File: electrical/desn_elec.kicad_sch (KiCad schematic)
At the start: 0 parts

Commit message: Update electrical
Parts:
- added BT1: Battery, symbol Device:Battery
- added J1: LOGITECH F310, symbol Connector:USB_A
- added M1, M2, M3: ESC_PWM, symbol PROJECT_SYM:ESC_PWM
- added U1: ESP32-S3-Zero, symbol PROJECT_SYM:ESP32-S3-Zero
- added U2: LM2596S-MOD, symbol PROJECT_SYM:LM2596S-MOD
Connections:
- new net: U1.18 (GND), U2. (VOUT)
- new net +5V: J1.4 (GND), J1.5 (Shield), U1.19 (5V), U1.22 (VBUS_USB), U2. (VOUT)
- new net +BATT: BT1.1 (+), M1.2 (+), M2.2 (+), M3.2 (+), U2. (VOUT)
- new net CONT_USB_D+: J1.3 (D+), U1.22 (VBUS_USB)
- new net CONT_USB_D-: J1.2 (D-), U1.22 (VBUS_USB)
- new net ESC_1: M1.4 (PWM), U1.3 (IO3)
- new net ESC_2: M2.4 (PWM), U1.2 (IO2)
- new net ESC_3: M3.4 (PWM), U1.1 (IO1)
- new net GND: BT1.2 (-), J1.1 (VBUS), M1.1 (-), M2.1 (-), M3.1 (-), U1.22 (VBUS_USB), U2. (VOUT)
- no-connect marks 0 -> 16

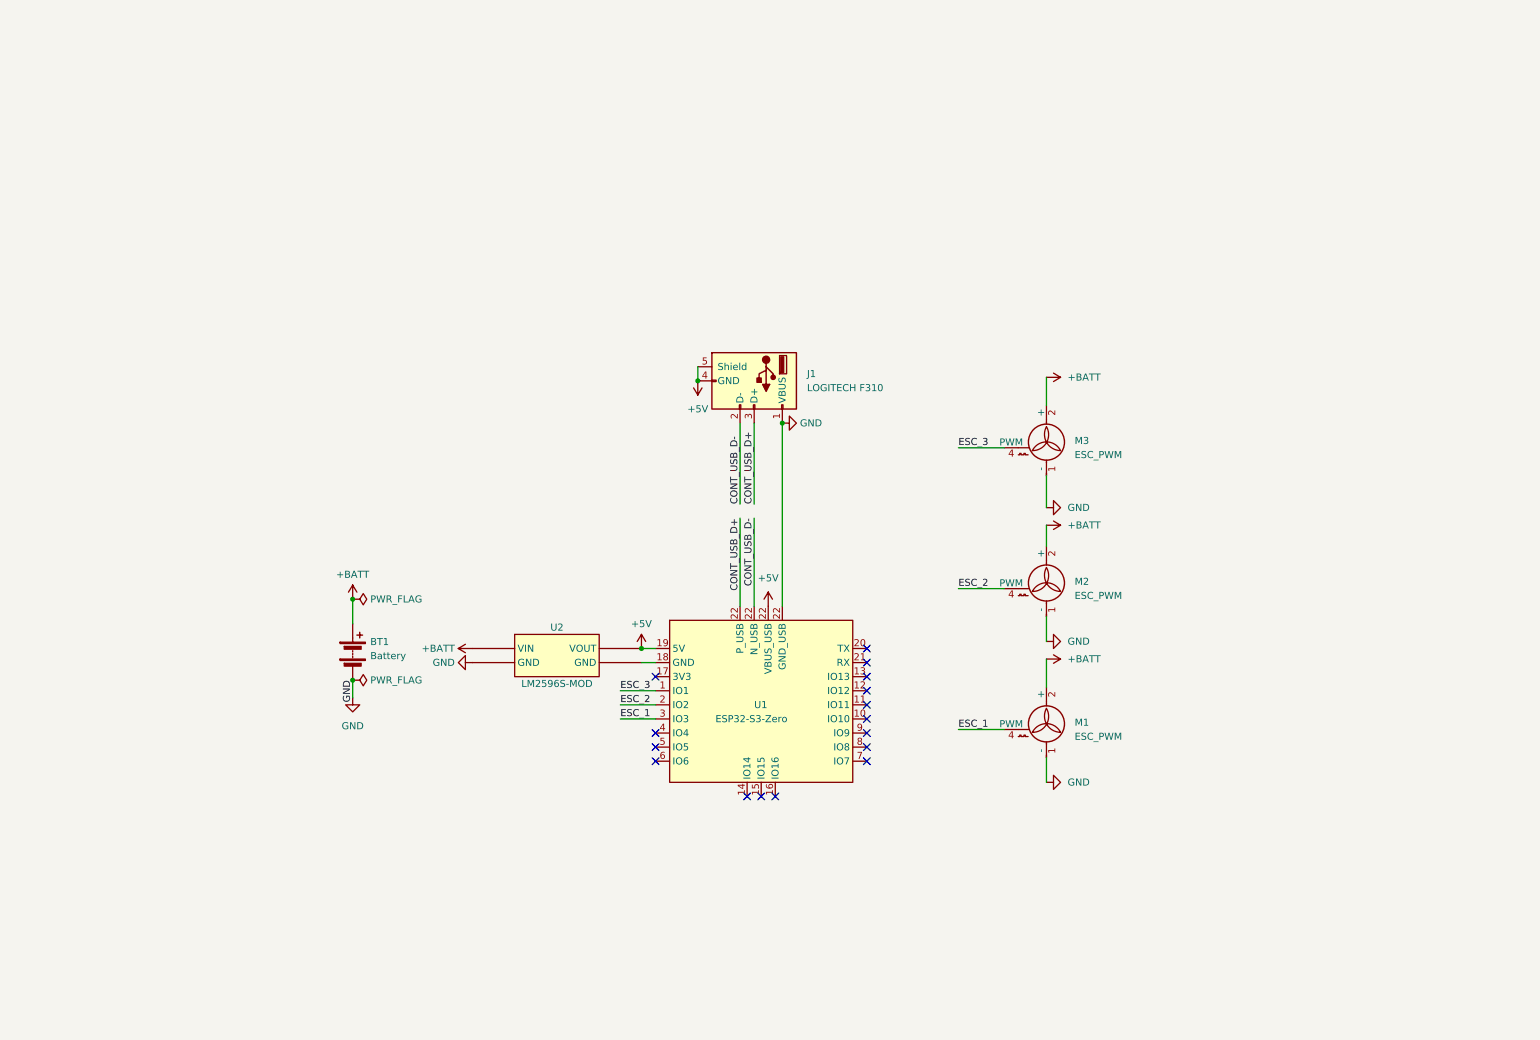
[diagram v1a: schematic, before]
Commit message: Update elec, make the diagram a bit nicer
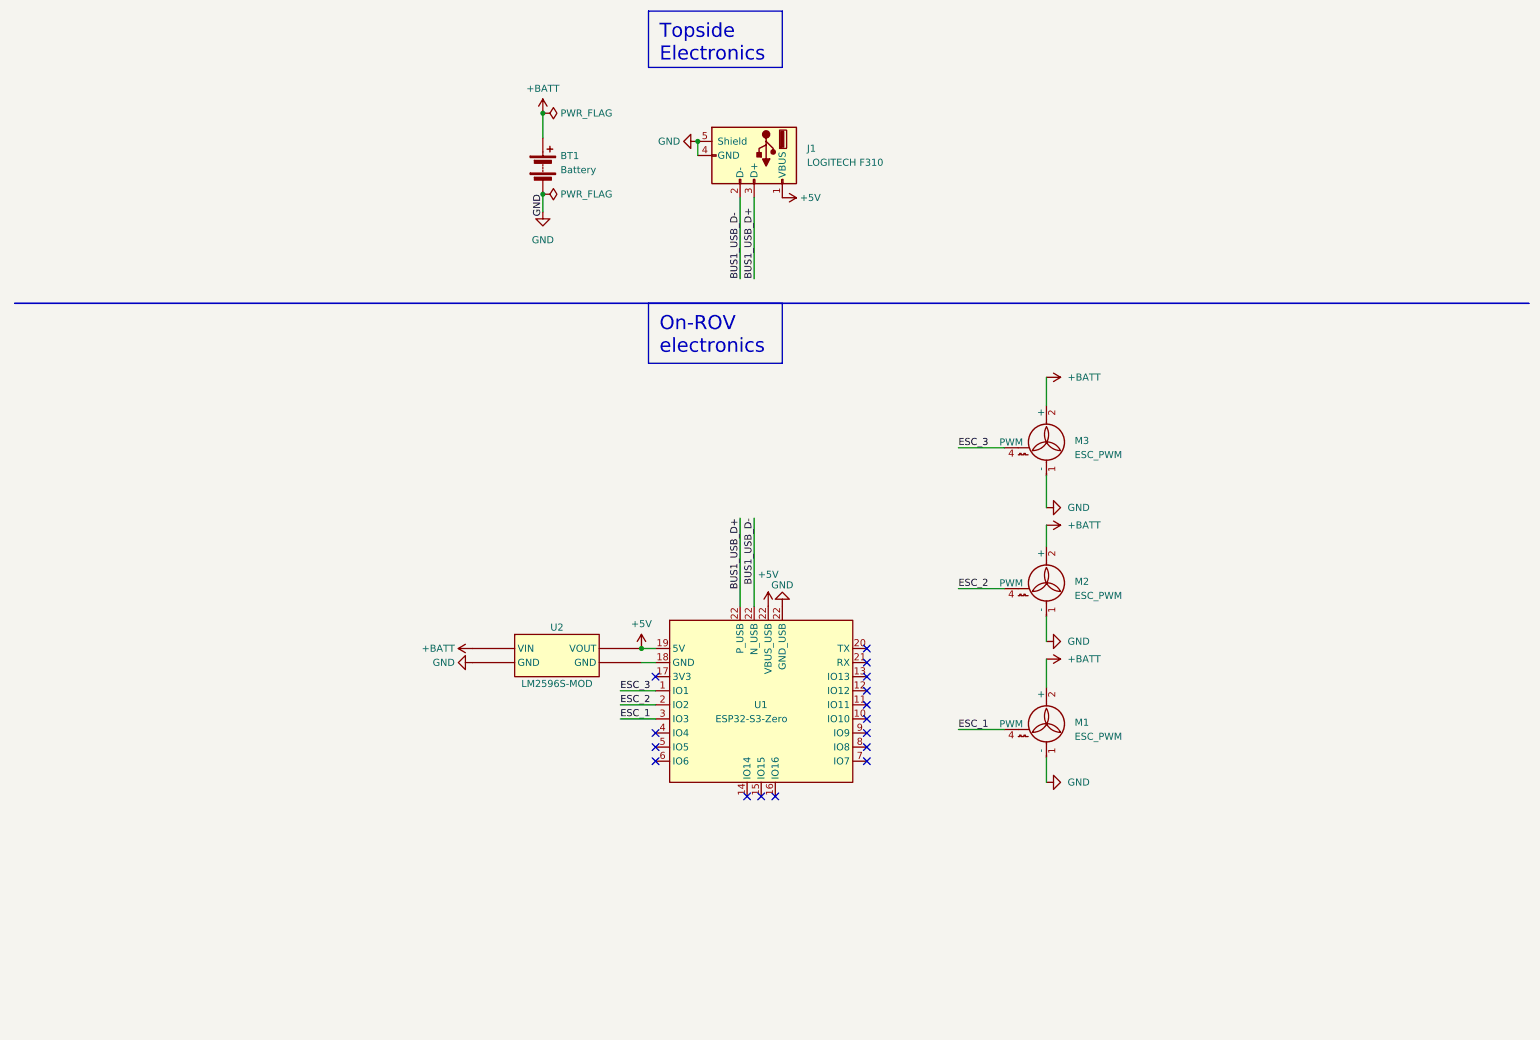
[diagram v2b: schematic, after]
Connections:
- net +5V: now also J1.1 (VBUS); no longer J1.4 (GND), J1.5 (Shield)
- net GND: now also J1.4 (GND), J1.5 (Shield); no longer J1.1 (VBUS)
- net CONT_USB_D+ renamed BUS1_USB_D+
- net CONT_USB_D- renamed BUS1_USB_D-
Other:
- moved on the sheet: BT1, J1

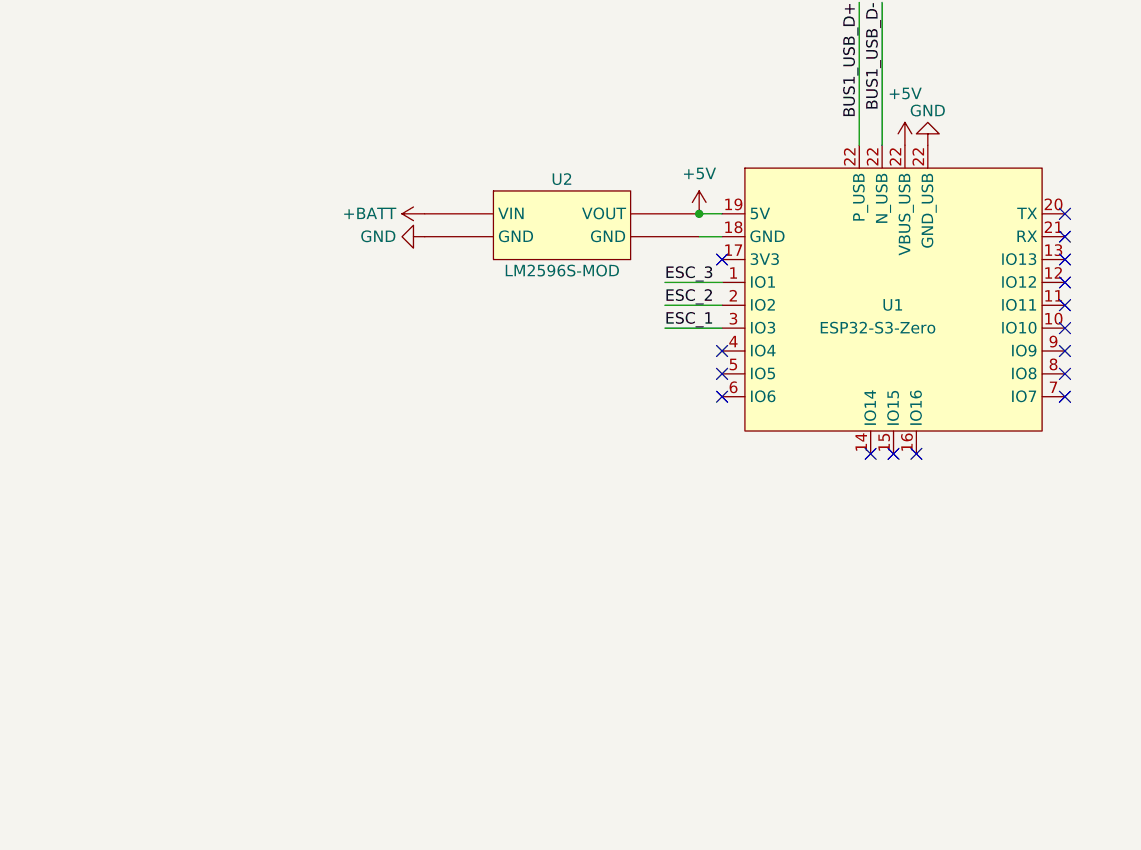
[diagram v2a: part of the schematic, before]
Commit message: Update electrical, add IMU (MP6050) on a breakout board
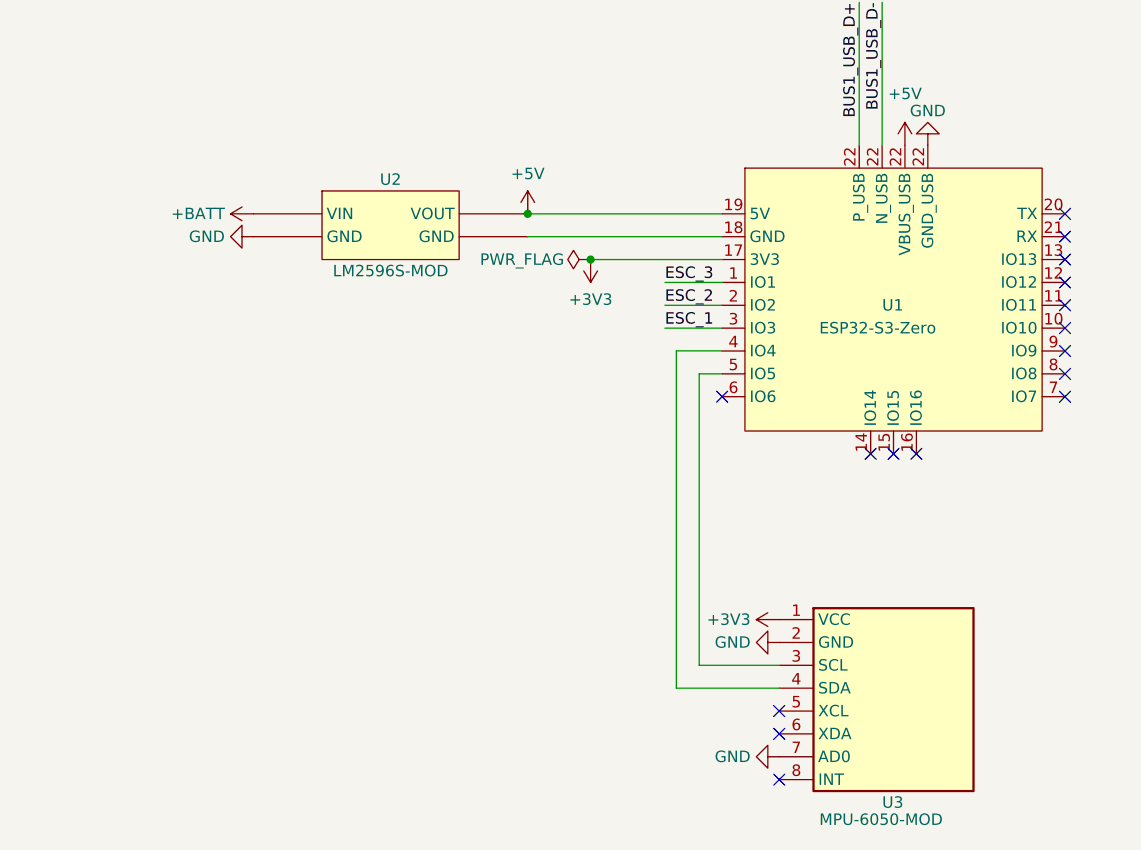
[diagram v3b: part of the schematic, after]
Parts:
- added U3: MPU-6050-MOD, Sensor_Motion:InvenSense_QFN-24_4x4mm_P0.5mm, symbol PROJECT_SYM:MPU-6050-MOD
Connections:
- net GND: now also U3.2 (GND), U3.7 (AD0)
- net +3V3: now reaches U1.17 (3V3)
- net +3V3: now also U3.1 (VCC)
- net at U1.4 (IO4): now also U3.4 (SDA)
- net at U1.5 (IO5): now also U3.3 (SCL)
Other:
- moved on the sheet: U2

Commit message: updates
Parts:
- removed U2: LM2596S-MOD, symbol PROJECT_SYM:LM2596S-MOD
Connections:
- net +5V: now also M1.5 (5V), M2.5 (5V), M3.5 (5V); no longer J1.1 (VBUS), U1.22 (VBUS_USB)
- net GND: now also M1.3 (GND), M2.3 (GND), M3.3 (GND), U1.18 (GND); no longer J1.4 (GND), J1.5 (Shield), U1.22 (VBUS_USB)
- net at U1.4 (IO4): no longer U3.4 (SDA)
- net at U1.5 (IO5): no longer U3.3 (SCL)
- new net: J1.1 (VBUS), U1.22 (VBUS_USB)
- new net: J1.4 (GND), J1.5 (Shield), U1.22 (VBUS_USB)
- new net IMU_SCL: U3.3 (SCL)
- new net IMU_SDA: U3.4 (SDA)
- no-connect marks 16 -> 18
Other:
- moved on the sheet: BT1, U1, U3
